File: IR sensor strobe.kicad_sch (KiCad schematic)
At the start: 22 parts, among them J1 CTL, J2 Sensors, J3 Conn_01x05, J4 Conn_01x02, Q1 NPN, Q2 OP550, Q3 OP550, Q4 OP550, Q5 OP550

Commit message: Add supply decoupling and CTL pull-down; move emitters/detectors off-board
Schematic and README work predating the oscillator change:

- Add C1 (10 uF) and C2 (0.1 uF) across the +5 V / GND entry at J4 to
  absorb the ~200 mA switching transient of the emitter array.
- Add R10 (10k) pull-down on CTL so the emitter array stays dark when
  CTL is undriven.
- D1-D4 (OP140) and Q2-Q5 (OP550) carry no footprints; they are remote
  parts wired through J5-J8. PCB nets renamed accordingly.
- README updated to match.

INCONSISTENT SNAPSHOT -- this revision is not a coherent design state.

The .kicad_pcb captured here had already been re-imported from the
*later* schematic, so it contains U1, R11, R12, C3-C5 and the DIN0207
resistor footprints, none of which exist in the .kicad_sch at this
commit. The schematic and board therefore disagree.

Do not build from, bisect to, or generate fabrication outputs from this
revision. The last coherent state before this work is 10a3dae; the next
coherent state is the following commit ("Add on-board 500 Hz strobe
oscillator; fix Q1 pinout; shrink resistors") and everything after it.
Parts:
- added C1: 10 uF, Capacitor_THT:CP_Radial_D5.0mm_P2.50mm, symbol Device:C_Polarized
- added C2: 0.1 uF, Capacitor_THT:C_Disc_D5.0mm_W2.5mm_P2.50mm, symbol Device:C
- added J5: OP550 return, Connector_PinHeader_2.54mm:PinHeader_1x04_P2.54mm_Vertical, symbol Connector_Generic:Conn_01x04
- added J6: OP550 out, Connector_PinHeader_2.54mm:PinHeader_1x04_P2.54mm_Vertical, symbol Connector_Generic:Conn_01x04
- added J7: OP140 in, Connector_PinHeader_2.54mm:PinHeader_1x04_P2.54mm_Vertical, symbol Connector_Generic:Conn_01x04
- added J8: OP140 out, Connector_PinHeader_2.54mm:PinHeader_1x04_P2.54mm_Vertical, symbol Connector_Generic:Conn_01x04
- added R10: 10k, Resistor_THT:R_Axial_DIN0411_L9.9mm_D3.6mm_P12.70mm_Horizontal, symbol Device:R
- D1, D2, D3, D4, Q2, Q3, Q4, Q5: footprint Connector_PinHeader_2.54mm:PinHeader_1x02_P2.54mm_Vertical -> (none)
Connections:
- net +5V: now also C1.1, C2.1
- net GND: now also C1.2, C2.2, J5.1 (Pin_1), J5.2 (Pin_2), J5.3 (Pin_3), J5.4 (Pin_4), R10.2
- net at J1.1 (Pin_1), R1.2: now also R10.1
- net at D1.2 (A), R2.2: now also J8.4 (Pin_4)
- net at J2.3 (Pin_3), Q4.1 (C), R8.2: now also J6.3 (Pin_3)
- net at J2.1 (Pin_1), Q2.1 (C), R6.2: now also J6.1 (Pin_1)
- net at J2.2 (Pin_2), Q3.1 (C), R7.2: now also J6.2 (Pin_2)
- net at J2.4 (Pin_4), Q5.1 (C), R9.2: now also J6.4 (Pin_4)
- net at D1.1 (K), D2.1 (K), D3.1 (K)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: now also J7.1 (Pin_1), J7.2 (Pin_2), J7.3 (Pin_3), J7.4 (Pin_4)
- net at D3.2 (A), R4.2: now also J8.2 (Pin_2)
- net at D4.2 (A), R5.2: now also J8.1 (Pin_1)
- net at D2.2 (A), R3.2: now also J8.3 (Pin_3)
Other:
- moved on the sheet: D1, D2, D3, D4, J2, J4, R2, R3, R4, R5

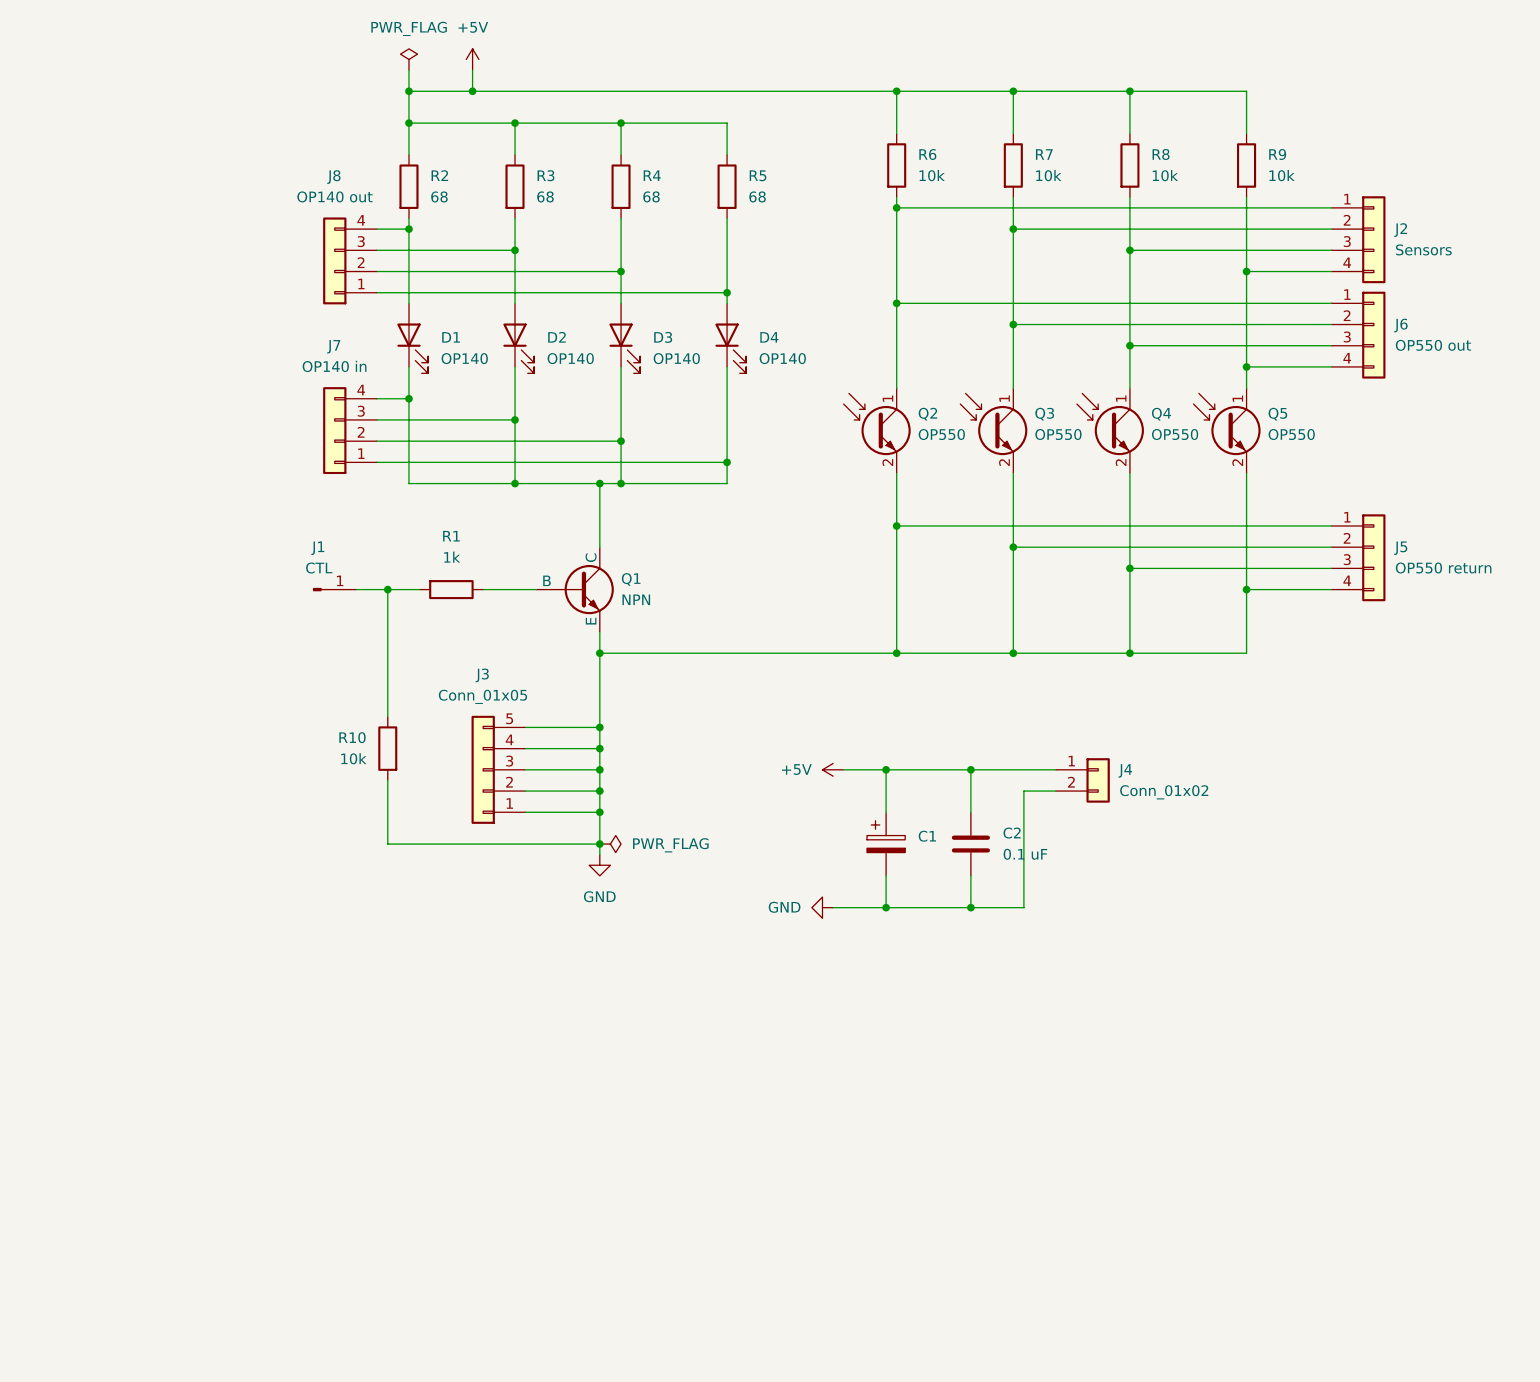
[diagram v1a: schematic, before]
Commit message: Add on-board 500 Hz strobe oscillator; fix Q1 pinout; shrink resistors
Lets the board self-strobe so the DAQ/sound-card analog output is no
longer needed to generate the carrier.

Oscillator:
- U1 TLC555 astable (R11 1k, R12 14k, C3 0.1 uF) -> 497 Hz at ~52% duty.
  f = 1.44 / ((R11 + 2*R12) * C3). C4 (0.01 uF) on CV, C5 (0.1 uF) local
  supply decoupling. RESET tied to +5 V.
- J1 becomes a 1x3 jumper: pin 1 OSC, pin 2 CTL, pin 3 EXT.
  Jumper 1-2 selects the on-board oscillator, 2-3 external drive.
  R10 still holds CTL low when the shunt is removed.
- R1 left at 1k so an external source (sound-card output) can still
  drive CTL without exceeding the TLC555's +/-10 mA output rating.

Q1 pinout fix:
- Swap Simulation_SPICE:NPN -> Device:Q_NPN_EBC, value set to 2N4401.
  The old symbol numbered pins 1=C, 2=B, 3=E, but a TO-92 2N4401 is
  1=E, 2=B, 3=C, so the netlist had collector and emitter transposed.
  Q1 would run reverse-active (beta_R ~5-20 instead of ~150), which is
  a likely cause of the low emitter output observed.
- NOTE: boards already fabricated from the previous netlist need Q1
  inserted rotated 180 degrees (flat face opposite the silkscreen).

Footprints:
- R1-R12 dropped from DIN0411 (12.70 mm pitch) to DIN0207 (7.62 mm),
  freeing roughly 390 mm^2 on the 1630 mm^2 board for the oscillator.
  Worst-case dissipation is 82 mW (R2-R5), well inside 1/4 W.

Verified with kicad-cli: ERC reports 0 errors. One warning remains,
global_label_dangling on EXT, which is intentional - that net leaves
the board through the jumper.
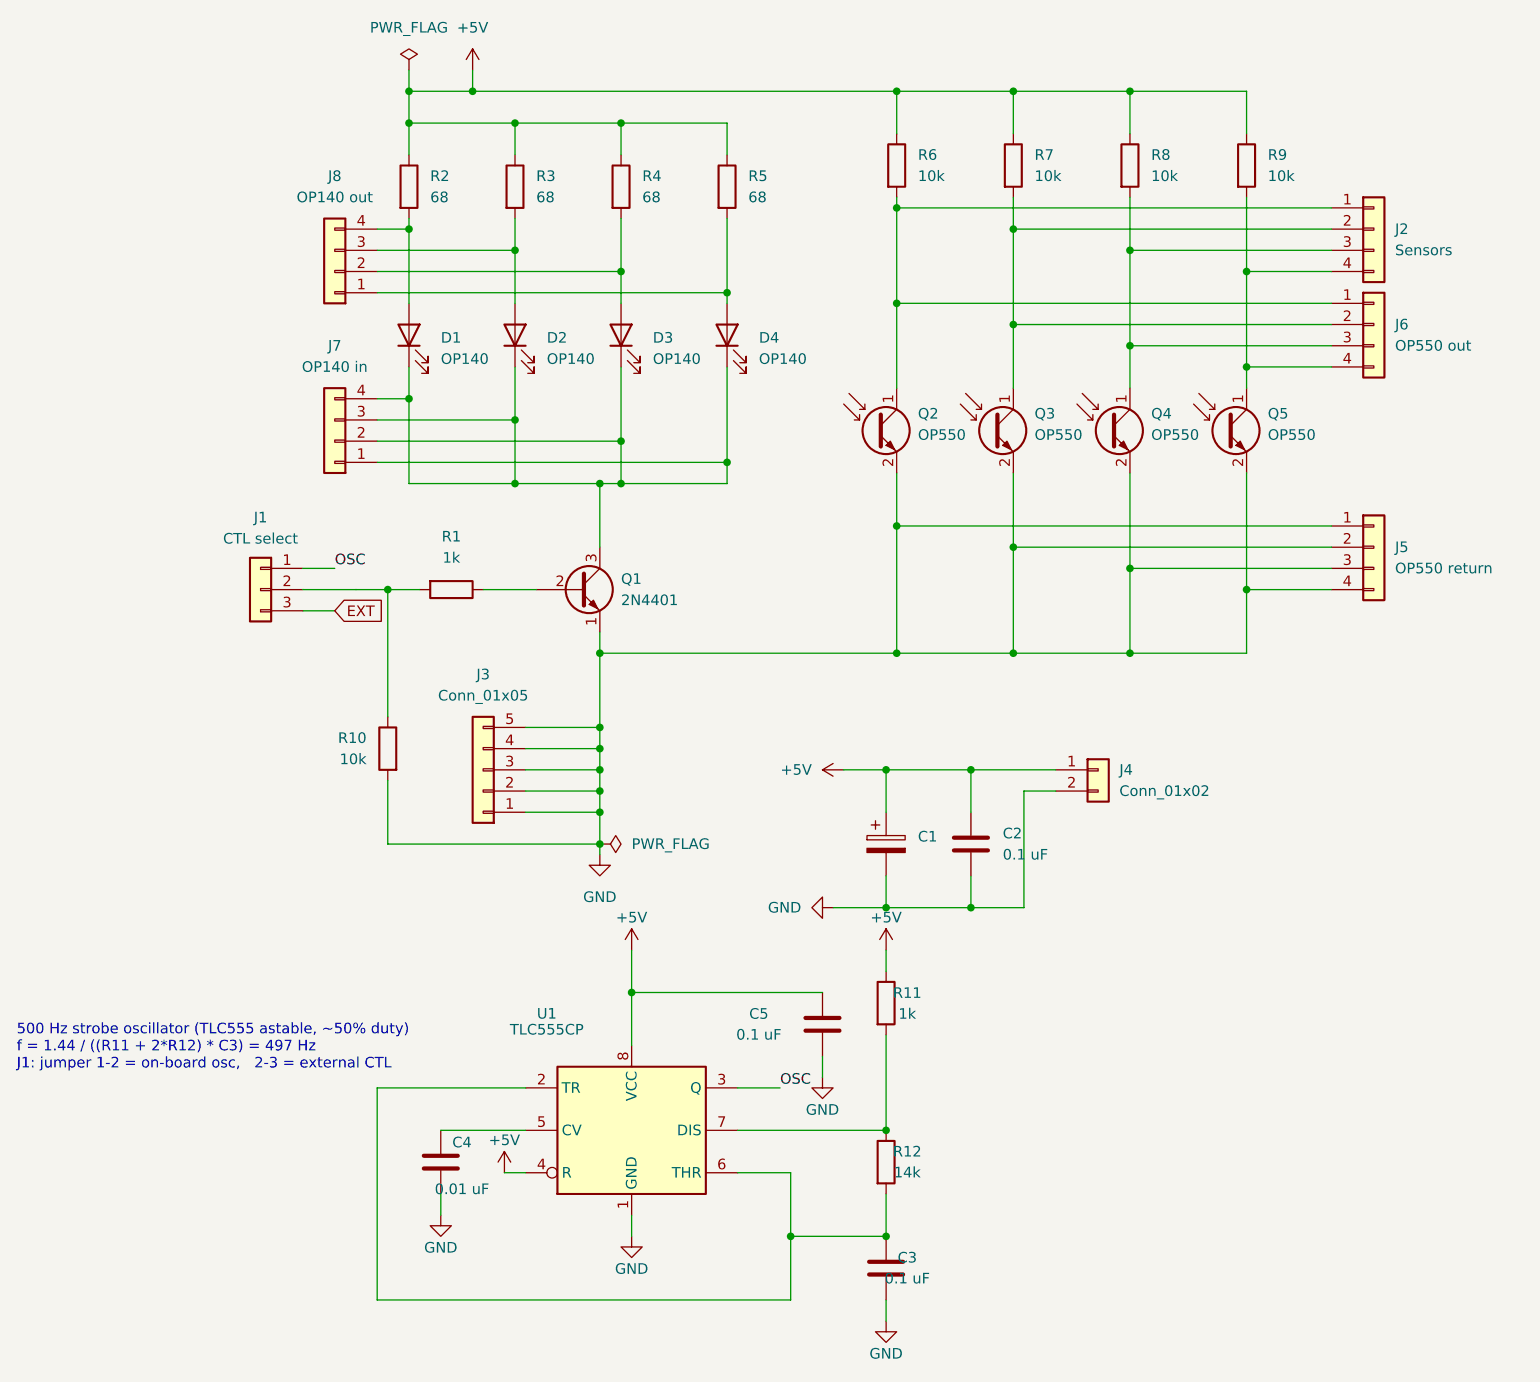
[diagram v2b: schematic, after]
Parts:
- removed J1: CTL, Connector_PinHeader_2.54mm:PinHeader_1x01_P2.54mm_Vertical, symbol Connector:Conn_01x01_Pin
- added C3, C5: 0.1 uF, Capacitor_THT:C_Disc_D5.0mm_W2.5mm_P2.50mm, symbol Device:C
- added C4: 0.01 uF, Capacitor_THT:C_Disc_D5.0mm_W2.5mm_P2.50mm, symbol Device:C
- added J1: CTL select, Connector_PinHeader_2.54mm:PinHeader_1x03_P2.54mm_Vertical, symbol Connector_Generic:Conn_01x03
- added R11: 1k, Resistor_THT:R_Axial_DIN0207_L6.3mm_D2.5mm_P7.62mm_Horizontal, symbol Device:R
- added R12: 14k, Resistor_THT:R_Axial_DIN0207_L6.3mm_D2.5mm_P7.62mm_Horizontal, symbol Device:R
- added U1: TLC555CP, Package_DIP:DIP-8_W7.62mm, symbol Timer:NE555P
- Q1: value NPN -> 2N4401; symbol Simulation_SPICE:NPN -> Device:Q_NPN_EBC
- R1, R10, R2, R3, R4, R5, R6, R7, R8, R9: footprint Resistor_THT:R_Axial_DIN0411_L9.9mm_D3.6mm_P12.70mm_Horizontal -> Resistor_THT:R_Axial_DIN0207_L6.3mm_D2.5mm_P7.62mm_Horizontal
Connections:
- net +5V: now also C5.1, R11.1, U1.4 (R), U1.8 (VCC)
- net GND: now also Q1.1 (E), C3.2, C4.2, C5.2, U1.1 (GND); no longer Q1.3 (E)
- net at R1.2, R10.1: now also J1.2 (Pin_2)
- net at D1.1 (K), D2.1 (K), D3.1 (K)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: now also Q1.3 (C); no longer Q1.1 (C)
- new net: R11.2, R12.1, U1.7 (DIS)
- new net: C3.1, R12.2, U1.2 (TR), U1.6 (THR)
- new net: C4.1, U1.5 (CV)
- new net EXT: J1.3 (Pin_3)
- new net OSC: J1.1 (Pin_1), U1.3 (Q)
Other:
- note added: "500 Hz strobe oscillator (TLC555 astable, ~50% duty) f = 1.44 / ((R11 + 2*R12) * C3) = 497 Hz J1: jumper 1-2 = on-board osc, 2-3 = external CTL"
